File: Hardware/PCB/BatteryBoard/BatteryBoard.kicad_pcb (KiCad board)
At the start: 2 copper layers, 60 x 60 mm, 55 parts, among them J1 USB_C_Receptacle_USB2.0, J2 Conn_01x07, J3 Conn_01x07, J4 Thermistor, J5 Conn_01x07, J6 Conn_01x07, J7 Power, Q1 TJ60S04M3L, SW1 SW_SPDT, U1 BQ25887RGER, U2 NJW4190M, U3 AZ1084C-3.3, U4 AZ1084C-5.0

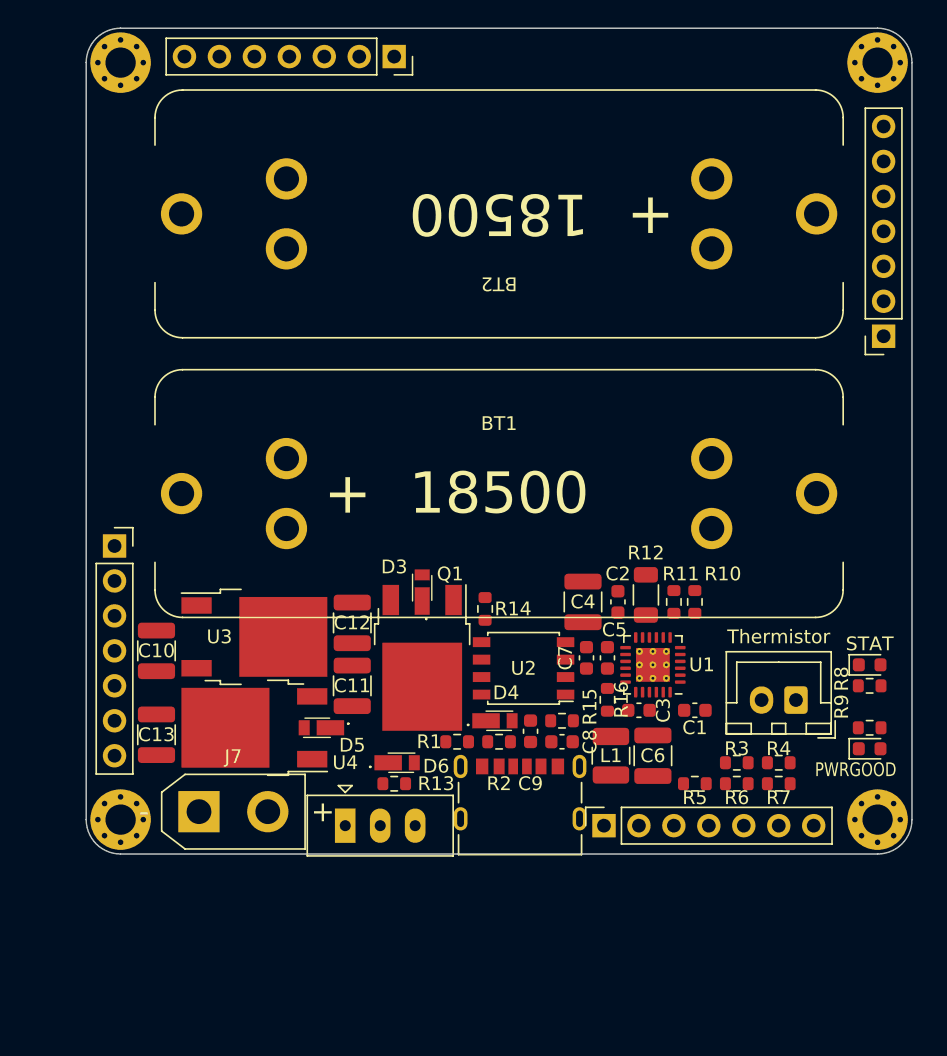
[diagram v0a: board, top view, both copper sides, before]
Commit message: 電源回路配置
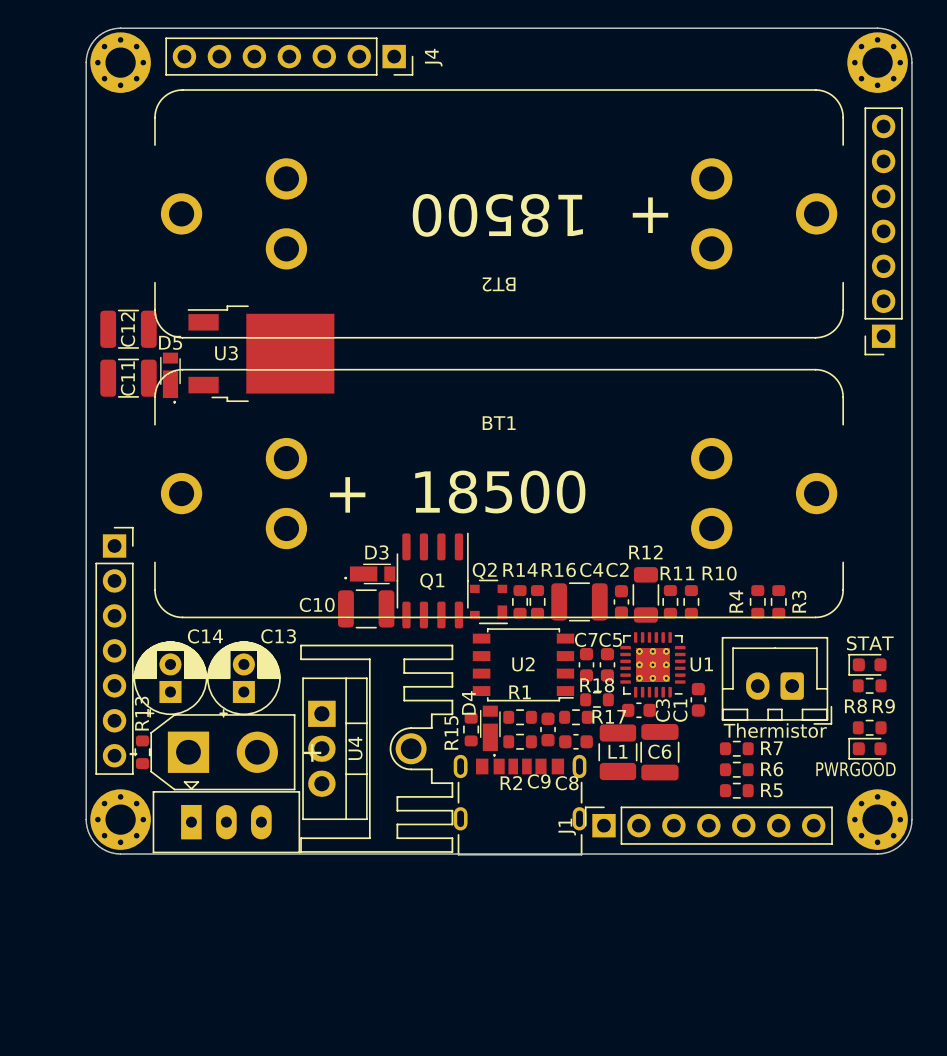
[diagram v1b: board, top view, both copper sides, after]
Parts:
- removed D6: D_Schottky, CUHS20S30:CUHS20S30
- added C14: 100uF, Capacitor_THT:CP_Radial_D5.0mm_P2.00mm, F.Cu at (126.1, 118.2)
- added HS1: Heatsink_Pad, Heatsink_extlib:Heatsink_15x11mm_11PB015, F.Cu at (140.6, 122.4)
- added Q2: BCV62, Package_TO_SOT_SMD:SOT-143, F.Cu at (149.2, 111.7)
- added R17: k, Resistor_SMD:R_0603_1608Metric, F.Cu at (155.6, 120.1)
- added R18: k, Resistor_SMD:R_0603_1608Metric, F.Cu at (157.1, 118.8)
- C13: value 22u(3225) -> 100uF; footprint Capacitor_SMD:C_1210_3225Metric -> Capacitor_THT:CP_Radial_D5.0mm_P2.00mm
- J1: value USB_C_Receptacle_USB2.0 -> Conn_01x07; footprint Kicad_Akiyuki_Footprint:CUI_UJC-HP-3-SMT-TR -> Connector_PinSocket_2.54mm:PinSocket_1x07_P2.54mm_Vertical
- J2: value Conn_01x07 -> USB_C_Receptacle_USB2.0; footprint Connector_PinSocket_2.54mm:PinSocket_1x07_P2.54mm_Vertical -> Kicad_Akiyuki_Footprint:CUI_UJC-HP-3-SMT-TR
- J4: value Thermistor -> Conn_01x07; footprint Connector_JST:JST_XH_B2B-XH-A_1x02_P2.50mm_Vertical -> Connector_PinSocket_2.54mm:PinSocket_1x07_P2.54mm_Vertical
- J5: value Conn_01x07 -> Thermistor; footprint Connector_PinSocket_2.54mm:PinSocket_1x07_P2.54mm_Vertical -> Connector_JST:JST_XH_B2B-XH-A_1x02_P2.50mm_Vertical
- Q1: value TJ60S04M3L -> FDS4935A; footprint Package_TO_SOT_SMD:TO-252-2 -> Package_SO:SOIC-8_3.9x4.9mm_P1.27mm
- R14: value 100 -> 10k
- R15: value k -> 100
- R16: value k -> 10k
- U4: value AZ1084C-5.0 -> MIC29500-5.0WT; footprint Package_TO_SOT_SMD:TO-252-2 -> Package_TO_SOT_THT:TO-220-3_Vertical
- moved J4 55.1 mm to (142.4, 72.1), turned to -90 degrees
- moved J5 54.1 mm to (171.3, 117.8), turned to 180 degrees
- moved D5 28.0 mm to (126.1, 94.9), turned to 90 degrees
- moved C11 27.6 mm to (123.1, 95.4), turned to 180 degrees
- moved C12 26.8 mm to (123.1, 91.9), turned to 180 degrees
- moved U3 20.6 mm to (132.7, 93.7)
- moved R13 18.4 mm to (124.1, 122.6), turned to 90 degrees
- moved C10 15.5 mm to (140.3, 112.2), turned to 180 degrees
- moved R3 12.1 mm to (170.3, 111.7), turned to 90 degrees
- moved R4 11.8 mm to (168.8, 111.7), turned to -90 degrees
- moved SW1 11.2 mm to (130.2, 127.7)
- moved R16 8.74 mm to (152.8, 111.7)
- moved J1 7.46 mm to (157.6, 127.9), turned to 90 degrees
- moved J2 7.46 mm to (151.5, 123.6), turned to 0 degrees
- moved C13 7.07 mm to (131.5, 118.2), turned to 90 degrees
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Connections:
- net Net-(C2-Pad1) renamed +5VREF
- C10 pad 1: +5V -> Net-(C10-Pad1)
- C11 pad 1: Net-(C11-Pad1) -> +5V
- D5 pad 1: Net-(C11-Pad1) -> +5V
- D5 pad 2: +5V -> +3.3V
- J4 pad 1: GND -> +5V
- J4 pad 2: TS -> GND
- J5 pad 1: +5V -> GND
- J5 pad 2: GND -> TS
- Q1 pad 1: Net-(Q1-Pad1) -> +5V
- Q1 pad 2: Net-(C11-Pad1) -> Net-(Q1-Pad2)
- R1 pad 1: Net-(J1-PadA5) -> Net-(J2-PadA5)
- R14 pad 1: Net-(Q1-Pad1) -> GND
- R14 pad 2: Net-(D4-Pad1) -> Net-(Q2-Pad1)
- R15 pad 1: GATE -> Net-(R15-Pad1)
- R15 pad 2: FB -> Net-(D4-Pad1)
- R16 pad 1: FB -> GND
- R16 pad 2: GND -> Net-(Q1-Pad2)
- R2 pad 1: Net-(J1-PadB5) -> Net-(J2-PadB5)
- R3 pad 2: VBUS -> +5V
- R5 pad 2: VBUS -> +3.3V
- R6 pad 2: VBUS -> +3.3V
- R7 pad 2: VBUS -> +3.3V
- R8 pad 2: VBUS -> +3.3V
- R9 pad 2: VBUS -> +3.3V
- U4 pad 1: GND -> Net-(C10-Pad1)
- U4 pad 2: +5V -> GND
- U4 pad 3: Net-(C11-Pad1) -> +5V

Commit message: Powerpathコンを使用、部品配置
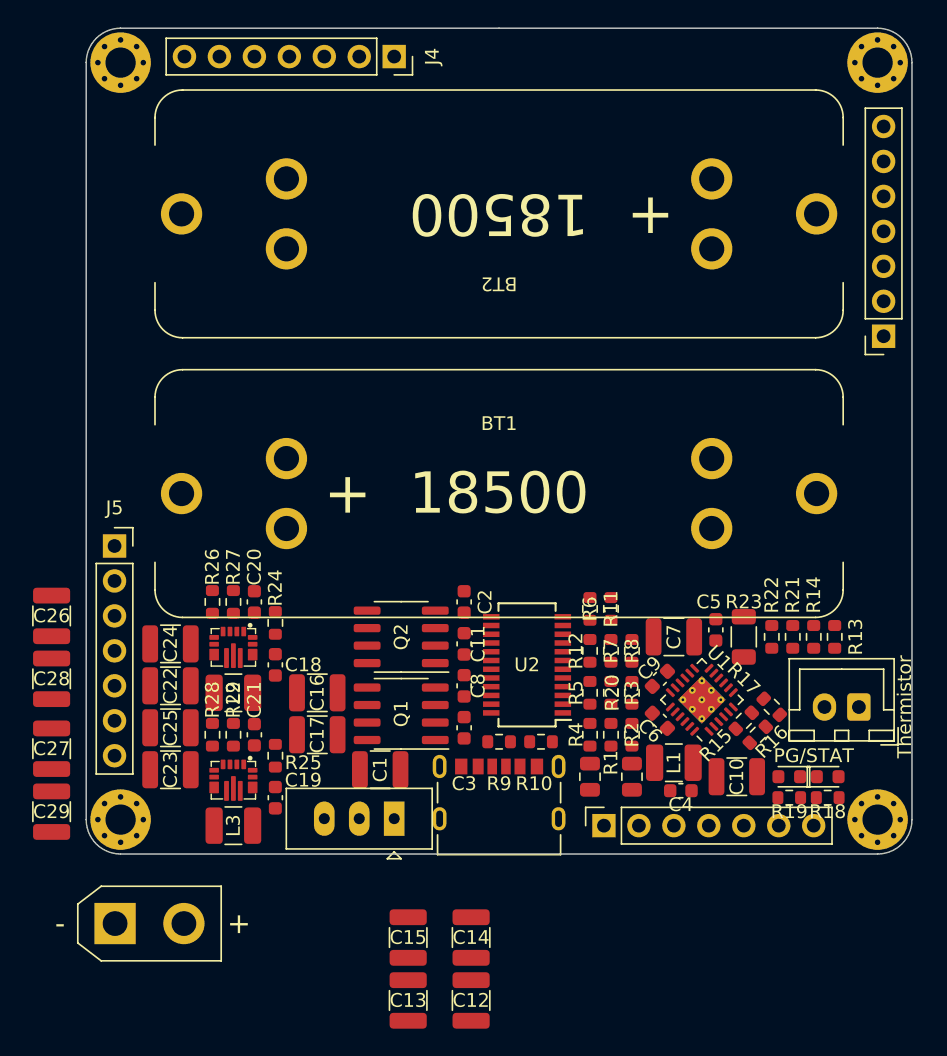
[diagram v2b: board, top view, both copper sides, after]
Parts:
- removed D3, D4, D5: D_Schottky, CUHS20S30:CUHS20S30
- removed HS1: Heatsink_Pad, Heatsink_extlib:Heatsink_15x11mm_11PB015
- added C15: 10u(3225), Capacitor_SMD:C_1210_3225Metric, F.Cu at (143.4, 136.1)
- added C16: 10u(3225), Capacitor_SMD:C_1210_3225Metric, F.Cu at (136.8, 118.3)
- added C17: 10u(3225), Capacitor_SMD:C_1210_3225Metric, F.Cu at (136.8, 121.3)
- added C18: 0.1u, Capacitor_SMD:C_0603_1608Metric, F.Cu at (133.7, 116.3)
- added C19: 0.1u, Capacitor_SMD:C_0603_1608Metric, F.Cu at (133.7, 125.9)
- added C20: 0.1u, Capacitor_SMD:C_0603_1608Metric, F.Cu at (132.2, 111.7)
- added C21: 0.1u, Capacitor_SMD:C_0603_1608Metric, F.Cu at (132.2, 121.3)
- added C22: 10u(3225), Capacitor_SMD:C_1210_3225Metric, F.Cu at (126.1, 117.8)
- added C23: 10u(3225), Capacitor_SMD:C_1210_3225Metric, F.Cu at (126.1, 123.9)
- added C24: 22u(3225), Capacitor_SMD:C_1210_3225Metric, F.Cu at (126.1, 114.7)
- added C25: 22u(3225), Capacitor_SMD:C_1210_3225Metric, F.Cu at (126.1, 120.8)
- added C26: 22u(3225), Capacitor_SMD:C_1210_3225Metric, F.Cu at (117.5, 112.7)
- added C27: 22u(3225), Capacitor_SMD:C_1210_3225Metric, F.Cu at (117.5, 122.4)
- added C28: 22u(3225), Capacitor_SMD:C_1210_3225Metric, F.Cu at (117.5, 117.3)
- added C29: 22u(3225), Capacitor_SMD:C_1210_3225Metric, F.Cu at (117.5, 126.9)
- added L2: 1uH, Inductor_SMD:L_1210_3225Metric, F.Cu at (130.7, 118.3)
- added L3: 1uH, Inductor_SMD:L_1210_3225Metric, F.Cu at (130.7, 127.9)
- added R19: 1k, Resistor_SMD:R_0603_1608Metric, F.Cu at (171.1, 125.9)
- added R20: 240k, Resistor_SMD:R_0603_1608Metric, F.Cu at (159.7, 118.3)
- added R21: 374, Resistor_SMD:R_0603_1608Metric, F.Cu at (171.3, 114.2)
- added R22: 330, Resistor_SMD:R_0603_1608Metric, F.Cu at (169.8, 114.2)
- added R23: 10(3216), Resistor_SMD:R_1206_3216Metric, F.Cu at (167.8, 114.2)
- added R24: 10k, Resistor_SMD:R_0603_1608Metric, F.Cu at (133.7, 113.2)
- added R25: 10k, Resistor_SMD:R_0603_1608Metric, F.Cu at (133.7, 122.9)
- added R26: 680k, Resistor_SMD:R_0603_1608Metric, F.Cu at (129.2, 111.7)
- added R27: 130k, Resistor_SMD:R_0603_1608Metric, F.Cu at (130.7, 111.7)
- added R28: 470k, Resistor_SMD:R_0603_1608Metric, F.Cu at (129.2, 121.3)
- added R29: 150k, Resistor_SMD:R_0603_1608Metric, F.Cu at (130.7, 121.3)
- added REF**: C_0805_2012Metric, Capacitor_SMD:C_0805_2012Metric, F.Cu at (156.6, 124.4)
- added REF**: C_0805_2012Metric, Capacitor_SMD:C_0805_2012Metric, F.Cu at (159.7, 124.4)
- C1, C7: value 1u -> 10u(3225); footprint Capacitor_SMD:C_0603_1608Metric -> Capacitor_SMD:C_1210_3225Metric
- C11: value 10u(3225) -> 0.1u; footprint Capacitor_SMD:C_1210_3225Metric -> Capacitor_SMD:C_0603_1608Metric
- C12: value 22u(3225) -> 10u(3225)
- C13, C14: value 100uF -> 10u(3225); footprint Capacitor_THT:CP_Radial_D5.0mm_P2.00mm -> Capacitor_SMD:C_1210_3225Metric
- C2: value 4.7u -> 0.1u
- C3: value 0.047u -> 0.1u
- C4: value 10u(3225) -> 1u; footprint Capacitor_SMD:C_1210_3225Metric -> Capacitor_SMD:C_0603_1608Metric
- C5: value 47p -> 4.7u
- C6: value 10u(3225) -> 0.047u; footprint Capacitor_SMD:C_1210_3225Metric -> Capacitor_SMD:C_0603_1608Metric
- C8: value 1u -> 0.1u
- C9: value 1u -> 47p
- J1: value Conn_01x07 -> USB_C_Receptacle_USB2.0; footprint Connector_PinSocket_2.54mm:PinSocket_1x07_P2.54mm_Vertical -> Kicad_Akiyuki_Footprint:CUI_UJC-HP-3-SMT-TR
- J2: value USB_C_Receptacle_USB2.0 -> Thermistor; footprint Kicad_Akiyuki_Footprint:CUI_UJC-HP-3-SMT-TR -> Connector_JST:JST_XH_B2B-XH-A_1x02_P2.50mm_Vertical
- J5: value Thermistor -> Conn_01x07; footprint Connector_JST:JST_XH_B2B-XH-A_1x02_P2.50mm_Vertical -> Connector_PinSocket_2.54mm:PinSocket_1x07_P2.54mm_Vertical
- Q2: value BCV62 -> FDS4935A; footprint Package_TO_SOT_SMD:SOT-143 -> Package_SO:SOIC-8_3.9x4.9mm_P1.27mm
- R1, R2: value 5.1k -> R_Small
- R10: value 374 -> 5.1k
- R11: value 330 -> R_Small
- R12: value 10(3216) -> R_Small; footprint Resistor_SMD:R_1206_3216Metric -> Resistor_SMD:R_0603_1608Metric
- R13: value 10k -> 5.11k
- R14: value 10k -> 30k
- R15: value 100 -> 4.7k
- R16: value 10k -> 4.7k
- R17: value k -> 4.7k
- R18: value k -> 1k
- R3: value 5.11k -> R_Small
- R4: value 30k -> R_Small
- R5, R6, R7: value 4.7k -> R_Small
- R8: value 1k -> R_Small
- R9: value 1k -> 5.1k
- U2: value NJW4190M -> LTC4417CGN; footprint Kicad_Akiyuki_Footprint:DMP-8_P1.27mm -> Package_SO:SSOP-24_3.9x8.7mm_P0.635mm
- U3: value AZ1084C-3.3 -> TPS63070; footprint Package_TO_SOT_SMD:TO-252-2 -> Module_SparkFun_Buck-Boost:VQFN-15-HR(3X2.5)
- U4: value MIC29500-5.0WT -> TPS63070; footprint Package_TO_SOT_THT:TO-220-3_Vertical -> Module_SparkFun_Buck-Boost:VQFN-15-HR(3X2.5)
- moved C12 54.8 mm to (148.0, 140.6), turned to -90 degrees
- moved R13 51.0 mm to (174.4, 114.2)
- moved J5 50.3 mm to (122.1, 107.6), turned to 0 degrees
- moved J3 41.0 mm to (157.6, 127.9), turned to 90 degrees
- moved C11 31.1 mm to (147.5, 114.7), turned to 90 degrees
- moved C10 29.6 mm to (167.3, 124.4), turned to 0 degrees
- moved C14 28.2 mm to (148.0, 136.1)
- moved R9 26.9 mm to (150.0, 121.8), turned to 0 degrees
- moved C13 25.4 mm to (143.4, 140.6), turned to -90 degrees
- moved J2 25.0 mm to (176.1, 119.3), turned to 180 degrees
- moved C1 23.7 mm to (141.4, 123.9), turned to 180 degrees
- moved R14 21.5 mm to (172.9, 114.2)
- moved U3 21.4 mm to (130.7, 115.0), turned to -90 degrees
- moved R15 19.8 mm to (167.8, 120.3), turned to 45 degrees
- moved R8 19.0 mm to (158.1, 115.2), turned to -90 degrees
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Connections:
- C10 pad 1: Net-(C10-Pad1) -> PMID
- C11 pad 1: +5V -> /VS2
- C12 pad 1: +3.3V -> VDD
- C13 pad 1: +5V -> VDD
- C14 pad 1: +5V -> VDD
- C2 pad 1: +5VREF -> +BATT
- C3 pad 1: Net-(C3-Pad1) -> VBUS
- C3 pad 2: SW -> GND
- C4 pad 1: +BATT -> VBUS
- C5 pad 1: Net-(C5-Pad1) -> +5VREF
- C6 pad 1: PMID -> Net-(C6-Pad1)
- C6 pad 2: GND -> SW
- C7 pad 1: Net-(C7-Pad1) -> +BATT
- C7 pad 2: Net-(C7-Pad2) -> GND
- C8 pad 1: VBUS -> /VS1
- C9 pad 1: GATE -> Net-(C9-Pad1)
- J3 pad 4: unconnected-(J3-Pad4) -> SDA
- J3 pad 5: unconnected-(J3-Pad5) -> SCL
- J3 pad 6: unconnected-(J3-Pad6) -> PSEL
- J3 pad 7: unconnected-(J3-Pad7) -> INT
- J5 pad 1: GND -> +5V
- J5 pad 2: TS -> GND
- Q1 pad 1: +5V -> /VS1
- Q1 pad 2: Net-(Q1-Pad2) -> /G1
- Q1 pad 3: +BATT -> /VS1
- Q1 pad 4: Net-(R15-Pad1) -> /G1
- Q1 pad 5: Net-(C10-Pad1) -> VBUS
- Q1 pad 6: Net-(C10-Pad1) -> VBUS
- Q1 pad 7: VBUS -> VDD
- Q1 pad 8: VBUS -> VDD
- Q2 pad 1: Net-(Q2-Pad1) -> /VS2
- Q2 pad 2: Net-(Q1-Pad2) -> /G2
- Q2 pad 3: +5V -> /VS2
- Q2 pad 4: VBUS -> /G2
- R1 pad 1: Net-(J2-PadA5) -> VBUS
- R1 pad 2: GND -> Net-(R1-Pad2)
- R10 pad 1: GND -> Net-(J1-PadB5)
- R10 pad 2: Net-(R10-Pad2) -> GND
- R11 pad 1: Net-(BT1-Pad2) -> /UV2
- R11 pad 2: MID -> Net-(R11-Pad2)
- R12 pad 1: Net-(BT1-Pad2) -> /OV2
- R12 pad 2: CBSET -> Net-(R12-Pad2)
- R13 pad 1: Net-(R13-Pad1) -> TS
- R13 pad 2: GND -> +5VREF
- R14 pad 2: Net-(Q2-Pad1) -> TS
- R15 pad 1: Net-(R15-Pad1) -> SDA
- R15 pad 2: Net-(D4-Pad1) -> +3.3V
- R16 pad 1: GND -> SCL
- R16 pad 2: Net-(Q1-Pad2) -> +3.3V
- R17 pad 1: GATE -> INT
- R17 pad 2: FB -> +3.3V
- R18 pad 1: FB -> Net-(D1-Pad2)
- R18 pad 2: GND -> +5VREF
- R2 pad 1: Net-(J2-PadB5) -> Net-(R1-Pad2)
- R2 pad 2: GND -> Net-(R2-Pad2)
- R3 pad 1: TS -> Net-(R2-Pad2)
- R3 pad 2: +5V -> GND
- R4 pad 1: GND -> /UV1
- R4 pad 2: TS -> Net-(R1-Pad2)
- R5 pad 1: SDA -> /OV1
- R5 pad 2: +3.3V -> Net-(R2-Pad2)
- R6 pad 1: SCL -> +BATT
- R6 pad 2: +3.3V -> Net-(R11-Pad2)
- R7 pad 1: INT -> Net-(R11-Pad2)
- R7 pad 2: +3.3V -> Net-(R12-Pad2)
- R8 pad 1: Net-(D1-Pad2) -> Net-(R12-Pad2)
- R8 pad 2: +3.3V -> GND
- R9 pad 1: Net-(D2-Pad2) -> Net-(J1-PadA5)
- R9 pad 2: +3.3V -> GND
- SW1 pad 1: Net-(R13-Pad1) -> GND
- SW1 pad 2: Net-(D4-Pad1) -> Net-(U2-Pad2)
- SW1 pad 3: Net-(D3-Pad1) -> unconnected-(SW1-Pad3)
- U1 pad 12: Net-(C3-Pad1) -> Net-(C6-Pad1)
- U1 pad 15: Net-(C5-Pad1) -> Net-(C9-Pad1)
- U1 pad 16: Net-(C5-Pad1) -> Net-(C9-Pad1)
- U1 pad 8: Net-(R10-Pad2) -> Net-(R21-Pad2)
- U2 pad 1: FB -> unconnected-(U2-Pad1)
- U2 pad 2: Net-(C7-Pad1) -> Net-(U2-Pad2)
- U2 pad 3: VBUS -> Net-(R20-Pad1)
- U2 pad 4: Net-(C7-Pad2) -> /UV1
- U2 pad 5: GND -> /OV1
- U2 pad 6: unconnected-(U2-Pad6) -> /UV2
- U2 pad 7: VBUS -> /OV2
- U2 pad 8: GATE -> GND
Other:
- outline, holes or cut-outs redrawn
- board text added: "PG/STAT"
- board text removed: "PWRGOOD"
- board text removed: "STAT"
